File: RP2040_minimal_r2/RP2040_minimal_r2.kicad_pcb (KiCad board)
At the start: 2 copper layers, 46 x 34 mm, 44 parts, among them J1 SPI0.8, J10 B20, J11 B21, J12 GPIO26-29, J2 SPI0.9, J3 SPI1.13, J4 I²C0, J5 USB, J6 B16, J7 B17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

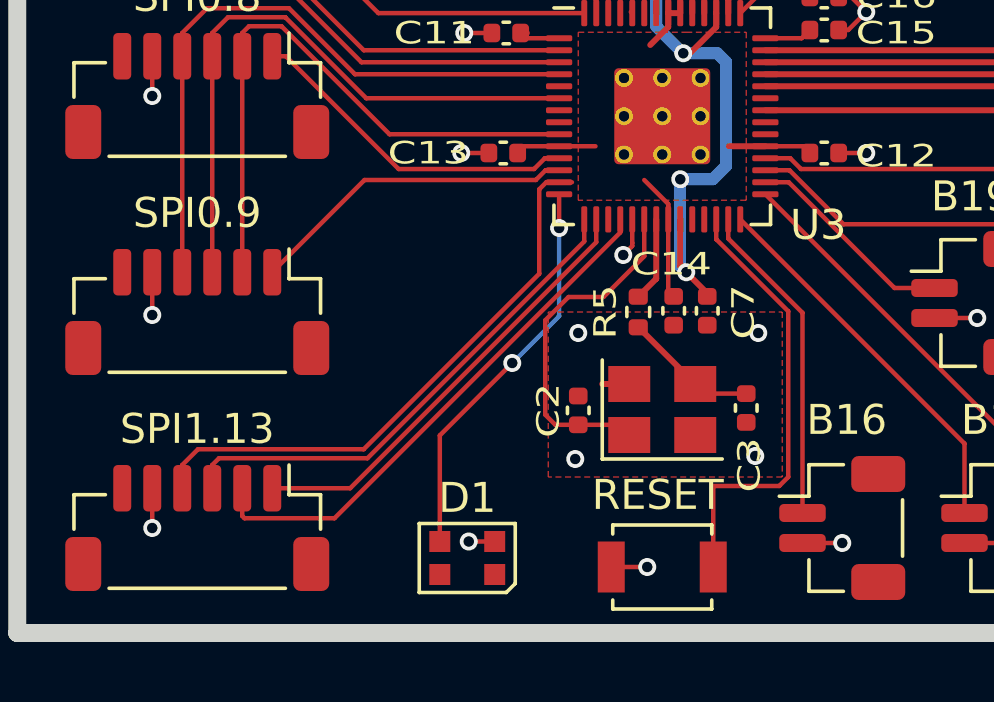
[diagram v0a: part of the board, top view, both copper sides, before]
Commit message: Add SWD debug connector.
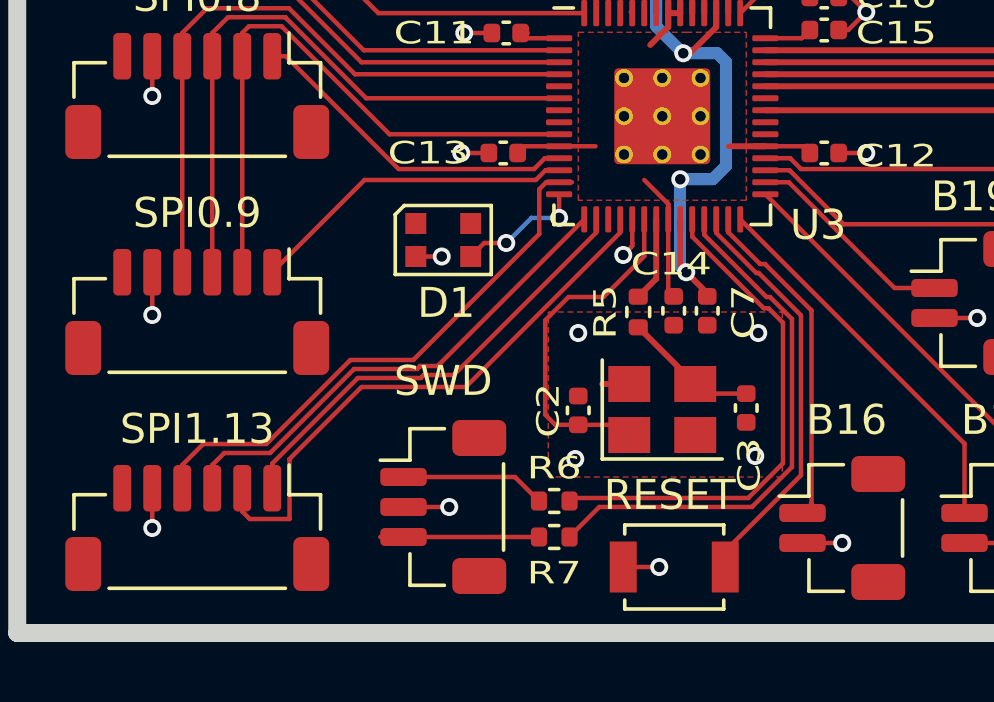
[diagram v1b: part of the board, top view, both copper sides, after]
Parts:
- added J13: SWD, RP2040_minimal:JST_SH_BM03B-SRSS-TB_1x03-1MP_P1.00mm_Vertical, F.Cu at (91.2, 99.8)
- added R6: 100, Resistor_SMD:R_0402_1005Metric, F.Cu at (94.9, 99.6)
- added R7: 100, Resistor_SMD:R_0402_1005Metric, F.Cu at (94.9, 100.8)
- moved D1 10.6 mm to (91.2, 90.9), turned to 0 degrees
- moved SW2 0.40 mm to (98.9, 101.8)
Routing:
- net /SWD: track 0.00 -> 17.9 mm
- net /SWCLK: track 0.00 -> 17.1 mm
- net /NEOPIXEL: track 13.3 -> 4.34 mm
- net Net-(J13-Pin_3): track 0.00 -> 5.29 mm
- net Net-(J13-Pin_1): track 0.00 -> 4.85 mm
- net GND: track 43.7 -> 45.2 mm, vias 31 -> 32
- net MOSI1: track 17.9 -> 19.0 mm
- net /RUN: track 14.9 -> 13.9 mm
- net SCLK1: track 19.3 -> 18.5 mm
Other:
- board text added: "github.com/monroewilliams/rp2040_mwtrackball version 1.0"
- board text removed: "github.com/monroewilliams/rp2040_mwtrackball"
